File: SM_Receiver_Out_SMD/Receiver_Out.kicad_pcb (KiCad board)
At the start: 2 copper layers, 83.2 x 71.4 mm, 66 parts, among them J1 String1, J10 SWD, J2 String2, J3 String3, J4 String4, J5 OLED, J6 VIN_Voltage, J7 RJ45, J8 RJ45, J9 Debug, SW1 ID, SW2 Terminators, SW3 User, SW4 RUN, U1 Pico, U2 AMS1117-5.0, U3 AM26C32IN, U4 74AHCT1G125, U5 74AHCT1G125, U6 74AHCT1G125, U7 74AHCT1G125

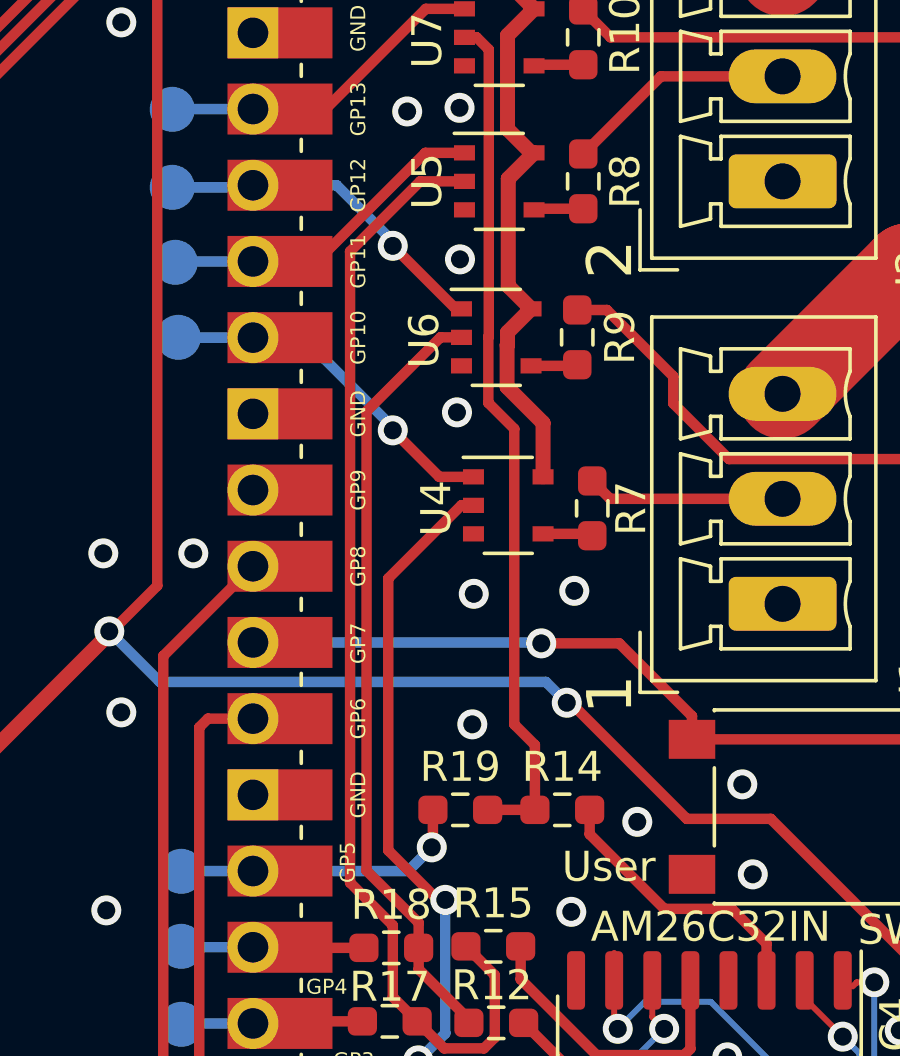
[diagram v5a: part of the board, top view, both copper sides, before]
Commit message: added 100 ohms
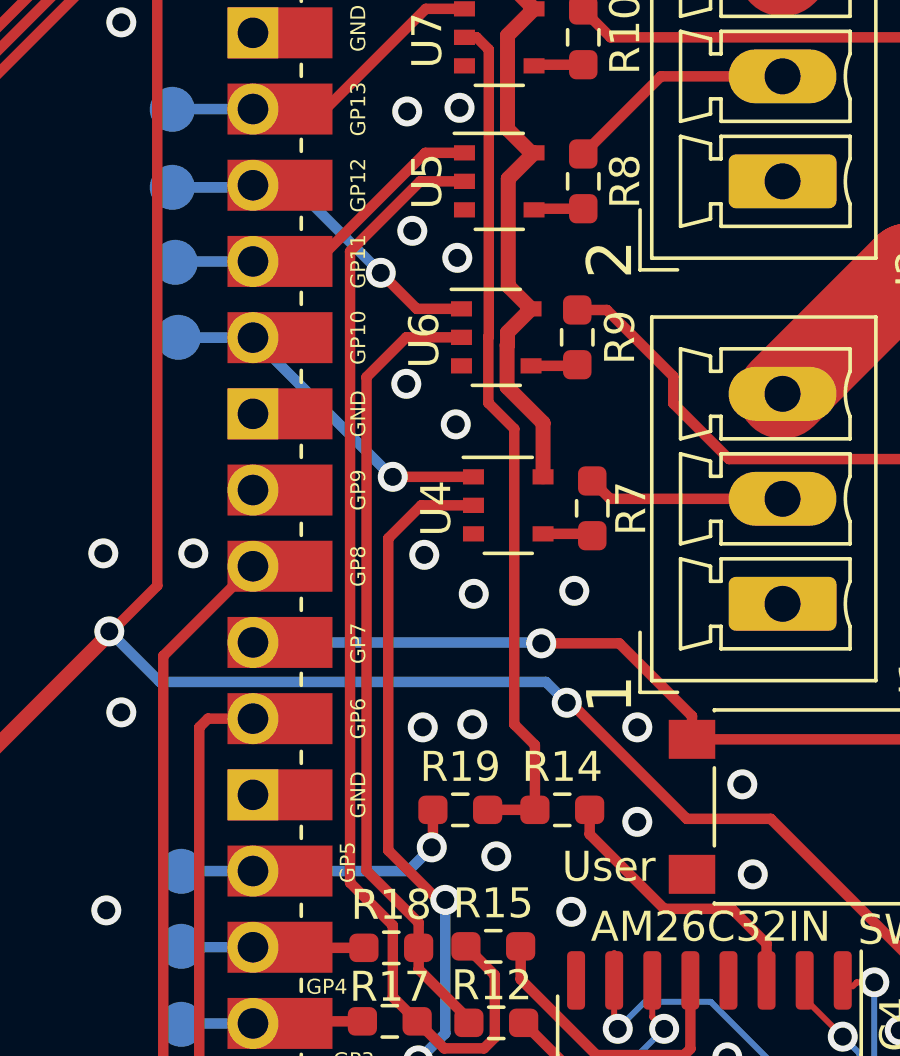
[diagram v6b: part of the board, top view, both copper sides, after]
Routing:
- net OUT17: track 24.2 -> 24.9 mm
- net OUT19: track 26.0 -> 26.7 mm
- net GND: vias 99 -> 105
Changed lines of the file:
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@@
   (title_block
     (title "SM Receiver")
-    (date "2022-04-29")
+    (date "2022-05-05")
     (rev "v2")
     (company "Scott Hanson")
@@
       (usegerberadvancedattributes false)
       (creategerberjobfile false)
+      (gerberprecision 5)
       (svguseinch false)
       (svgprecision 6)
@@
   )
   (via (at 94.401 98.1178) (size 1) (drill 0.6) (layers "F.Cu" "B.Cu") (free) (net 1))
+  (via (at 72.751 122.2178) (size 1) (drill 0.6) (layers "F.Cu" "B.Cu") (free) (net 1))
   (via (at 53.301 94.4178) (size 1) (drill 0.6) (layers "F.Cu" "B.Cu") (free) (net 1))
   (via (at 102.701 150.2178) (size 1) (drill 0.6) (layers "F.Cu" "B.Cu") (free) (net 1))
   (via (at 108.701 133.6178) (size 1) (drill 0.6) (layers "F.Cu" "B.Cu") (free) (net 1))
-  (via (at 73.991011 106.6178) (size 1) (drill 0.6) (layers "F.Cu" "B.Cu") (free) (net 1))
+  (via (at 73.901 106.5678) (size 1) (drill 0.6) (layers "F.Cu" "B.Cu") (free) (net 1))
   (via (at 97.201 89.8178) (size 1) (drill 0.6) (layers "F.Cu" "B.Cu") (free) (net 1))
-  (via (at 73.891011 111.7178) (size 1) (drill 0.6) (layers "F.Cu" "B.Cu") (free) (net 1))
+  (via (at 73.851 112.1178) (size 1) (drill 0.6) (layers "F.Cu" "B.Cu") (free) (net 1))
   (via (at 104.201 83.5328) (size 1) (drill 0.6) (layers "F.Cu" "B.Cu") (free) (net 1))
   (via (at 101.881 125.8378) (size 1) (drill 0.6) (layers "F.Cu" "B.Cu") (free) (net 1))
@@
   (via (at 114.301 92.1178) (size 1) (drill 0.6) (layers "F.Cu" "B.Cu") (free) (net 1))
   (via (at 108.801 139.1178) (size 1) (drill 0.6) (layers "F.Cu" "B.Cu") (free) (net 1))
+  (via (at 72.801 116.4678) (size 1) (drill 0.6) (layers "F.Cu" "B.Cu") (free) (net 1))
+  (via (at 72.401 105.6678) (size 1) (drill 0.6) (layers "F.Cu" "B.Cu") (free) (net 1))
   (via (at 118.301 141.8178) (size 1) (drill 0.6) (layers "F.Cu" "B.Cu") (free) (net 1))
   (via (at 63.501 140.5178) (size 1) (drill 0.6) (layers "F.Cu" "B.Cu") (free) (net 1))
@@
   (via (at 97.901 150.2178) (size 1) (drill 0.6) (layers "F.Cu" "B.Cu") (free) (net 1))
   (via (at 72.231 101.6878) (size 1) (drill 0.6) (layers "F.Cu" "B.Cu") (free) (net 1))
+  (via (at 72.201 110.7678) (size 1) (drill 0.6) (layers "F.Cu" "B.Cu") (free) (net 1))
   (via (at 113.301 130.0178) (size 1) (drill 0.6) (layers "F.Cu" "B.Cu") (free) (net 1))
   (via (at 88.651 132.3178) (size 1) (drill 0.6) (layers "F.Cu" "B.Cu") (free) (net 1))
@@
   (via (at 84.101 150.3178) (size 1) (drill 0.6) (layers "F.Cu" "B.Cu") (free) (net 1))
   (via (at 94.301 112.2178) (size 1) (drill 0.6) (layers "F.Cu" "B.Cu") (free) (net 1))
+  (via (at 79.901 122.2178) (size 1) (drill 0.6) (layers "F.Cu" "B.Cu") (free) (net 1))
   (via (at 62.701 98.7178) (size 1) (drill 0.6) (layers "F.Cu" "B.Cu") (free) (net 1))
   (via (at 78.551 137.9178) (size 1) (drill 0.6) (layers "F.Cu" "B.Cu") (free) (net 1))
@@
   (via (at 118.601 143.6178) (size 1) (drill 0.6) (layers "F.Cu" "B.Cu") (free) (net 1))
   (via (at 110.201 129.9178) (size 1) (drill 0.6) (layers "F.Cu" "B.Cu") (free) (net 1))
+  (via (at 75.201 126.5178) (size 1) (drill 0.6) (layers "F.Cu" "B.Cu") (free) (net 1))
   (via (at 110.201 128.6178) (size 1) (drill 0.6) (layers "F.Cu" "B.Cu") (free) (net 1))
   (via (at 62.101 145.0178) (size 1) (drill 0.6) (layers "F.Cu" "B.Cu") (free) (net 1))
@@
   (segment (start 74.141 99.2178) (end 74.545022 99.2178) (width 0.35) (layer "F.Cu") (net 4))
   (segment (start 74.2885 131.9553) (end 72.6135 130.2803) (width 0.35) (layer "F.Cu") (net 5))
-  (segment (start 70.876499 111.682301) (end 70.876499 126.993299) (width 0.35) (layer "F.Cu") (net 5))
-  (segment (start 74.041 109.2178) (end 73.341 109.2178) (width 0.35) (layer "F.Cu") (net 5))
-  (segment (start 72.6135 128.7303) (end 72.6135 129.5678) (width 0.35) (layer "F.Cu") (net 5))
+  (segment (start 70.876499 110.542301) (end 70.876499 126.993299) (width 0.35) (layer "F.Cu") (net 5))
   (segment (start 74.2885 132.0678) (end 74.2885 131.9553) (width 0.35) (layer "F.Cu") (net 5))
   (segment (start 72.6135 130.2803) (end 72.6135 129.5678) (width 0.35) (layer "F.Cu") (net 5))
+  (segment (start 72.6135 128.7303) (end 72.6135 129.5678) (width 0.35) (layer "F.Cu") (net 5))
+  (segment (start 72.201 109.2178) (end 70.876499 110.542301) (width 0.35) (layer "F.Cu") (net 5))
   (segment (start 70.876499 126.993299) (end 72.6135 128.7303) (width 0.35) (layer "F.Cu") (net 5))
-  (segment (start 73.341 109.2178) (end 70.876499 111.682301) (width 0.35) (layer "F.Cu") (net 5))
+  (segment (start 74.041 109.2178) (end 72.201 109.2178) (width 0.35) (layer "F.Cu") (net 5))
   (segment (start 70.326989 106.355079) (end 70.326989 127.393789) (width 0.35) (layer "F.Cu") (net 6))
   (segment (start 75.15148 132.557846) (end 74.792006 132.91732) (width 0.35) (layer "F.Cu") (net 6))
@@
   (segment (start 74.141 104.0178) (end 72.664268 104.0178) (width 0.35) (layer "F.Cu") (net 6))
   (segment (start 71.75148 128.81828) (end 71.75148 131.20578) (width 0.35) (layer "F.Cu") (net 6))
-  (segment (start 73.251 127.9678) (end 73.501 127.9678) (width 0.35) (layer "F.Cu") (net 7))
   (segment (start 72.5635 134.6678) (end 72.5635 133.3553) (width 0.35) (layer "F.Cu") (net 7))
   (segment (start 72.5635 133.3553) (end 72.601 133.3178) (width 0.35) (layer "F.Cu") (net 7))
+  (segment (start 71.601 115.9178) (end 71.601 126.3178) (width 0.35) (layer "F.Cu") (net 7))
   (segment (start 71.601 126.3178) (end 73.251 127.9678) (width 0.35) (layer "F.Cu") (net 7))
-  (segment (start 74.441 114.8178) (end 74.036978 114.8178) (width 0.35) (layer "F.Cu") (net 7))
-  (segment (start 74.036978 114.8178) (end 71.601 117.253778) (width 0.35) (layer "F.Cu") (net 7))
+  (segment (start 73.251 127.9678) (end 73.501 127.9678) (width 0.35) (layer "F.Cu") (net 7))
   (segment (start 72.5635 134.6678) (end 74.1385 134.6678) (width 0.35) (layer "F.Cu") (net 7))
-  (segment (start 71.601 117.253778) (end 71.601 126.3178) (width 0.35) (layer "F.Cu") (net 7))
+  (segment (start 72.701 114.8178) (end 71.601 115.9178) (width 0.35) (layer "F.Cu") (net 7))
+  (segment (start 74.441 114.8178) (end 72.701 114.8178) (width 0.35) (layer "F.Cu") (net 7))
   (via (at 73.501 127.9678) (size 1) (drill 0.6) (layers "F.Cu" "B.Cu") (net 7))
   (via (at 72.601 133.3178) (size 1) (drill 0.6) (layers "F.Cu" "B.Cu") (net 7))
@@
   (segment (start 114.501 86.6028) (end 115.736 86.6028) (width 1) (layer "F.Cu") (net 27))
   (segment (start 67.3885 145.9178) (end 65.476 145.9178) (width 0.35) (layer "F.Cu") (net 28))
-  (segment (start 73.301 113.8678) (end 71.751 112.3178) (width 0.35) (layer "F.Cu") (net 29))
-  (segment (start 74.441 113.8678) (end 73.301 113.8678) (width 0.35) (layer "F.Cu") (net 29))
-  (via (at 71.751 112.3178) (size 1) (drill 0.6) (layers "F.Cu" "B.Cu") (net 29))
+  (segment (start 74.441 113.8678) (end 71.751 113.8678) (width 0.35) (layer "F.Cu") (net 29))
+  (via (at 71.751 113.8678) (size 1) (drill 0.6) (layers "F.Cu" "B.Cu") (net 29))
   (segment (start 67.091 109.2278) (end 64.611 109.2278) (width 0.35) (layer "B.Cu") (net 29))
-  (segment (start 71.751 112.2178) (end 71.751 112.3178) (width 0.35) (layer "B.Cu") (net 29))
   (segment (start 64.611 109.2278) (end 64.601 109.2178) (width 0.35) (layer "B.Cu") (net 29))
-  (segment (start 68.761 109.2278) (end 71.751 112.2178) (width 0.35) (layer "B.Cu") (net 29))
-  (segment (start 67.091 109.2278) (end 68.761 109.2278) (width 0.35) (layer "B.Cu") (net 29))
+  (segment (start 67.091 109.2278) (end 71.731 113.8678) (width 0.35) (layer "B.Cu") (net 29))
+  (segment (start 71.731 113.8678) (end 71.751 113.8678) (width 0.35) (layer "B.Cu") (net 29))
   (segment (start 74.141 103.0678) (end 72.837143 103.0678) (width 0.35) (layer "F.Cu") (net 30))
   (segment (start 72.837143 103.0678) (end 69.217143 106.6878) (width 0.35) (layer "F.Cu") (net 30))
@@
   (segment (start 64.531 106.6878) (end 64.501 106.7178) (width 0.35) (layer "B.Cu") (net 30))
   (segment (start 67.091 106.6878) (end 64.531 106.6878) (width 0.35) (layer "B.Cu") (net 30))
-  (segment (start 74.041 108.2678) (end 73.851 108.2678) (width 0.35) (layer "F.Cu") (net 31))
-  (segment (start 73.851 108.2678) (end 71.751 106.1678) (width 0.35) (layer "F.Cu") (net 31))
-  (via (at 71.751 106.1678) (size 1) (drill 0.6) (layers "F.Cu" "B.Cu") (net 31))
-  (segment (start 71.751 106.0178) (end 71.751 106.1678) (width 0.35) (layer "B.Cu") (net 31))
+  (segment (start 74.041 108.2678) (end 72.551 108.2678) (width 0.35) (layer "F.Cu") (net 31))
+  (segment (start 72.551 108.2678) (end 71.351 107.0678) (width 0.35) (layer "F.Cu") (net 31))
+  (via (at 71.351 107.0678) (size 1) (drill 0.6) (layers "F.Cu" "B.Cu") (net 31))
+  (segment (start 68.431 104.1478) (end 71.351 107.0678) (width 0.35) (layer "B.Cu") (net 31))
   (segment (start 64.401 104.2178) (end 67.021 104.2178) (width 0.35) (layer "B.Cu") (net 31))
-  (segment (start 69.881 104.1478) (end 71.751 106.0178) (width 0.35) (layer "B.Cu") (net 31))
-  (segment (start 67.091 104.1478) (end 69.881 104.1478) (width 0.35) (layer "B.Cu") (net 31))
+  (segment (start 67.091 104.1478) (end 68.431 104.1478) (width 0.35) (layer "B.Cu") (net 31))
   (segment (start 67.021 104.2178) (end 67.091 104.1478) (width 0.35) (layer "B.Cu") (net 31))
   (segment (start 72.851 98.2678) (end 69.511 101.6078) (width 0.35) (layer "F.Cu") (net 32))

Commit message: added logo
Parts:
- added G***: LOGO, Scotts:chewi_15, B.Cu at (57.9, 147.1)
